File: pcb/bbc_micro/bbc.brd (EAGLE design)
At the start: 52 x 55 mm, 16 parts, among them J1 ATX24RH

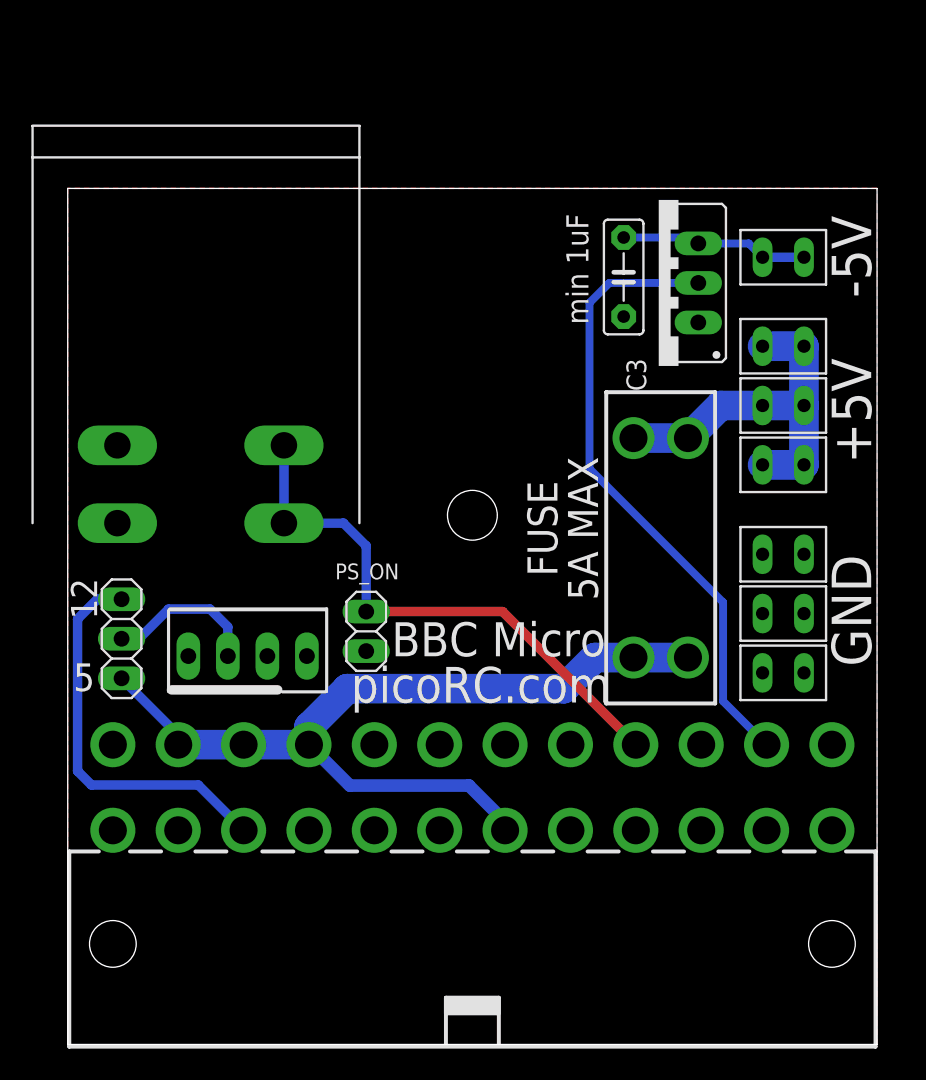
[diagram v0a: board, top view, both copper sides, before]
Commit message: added one more -5v rail
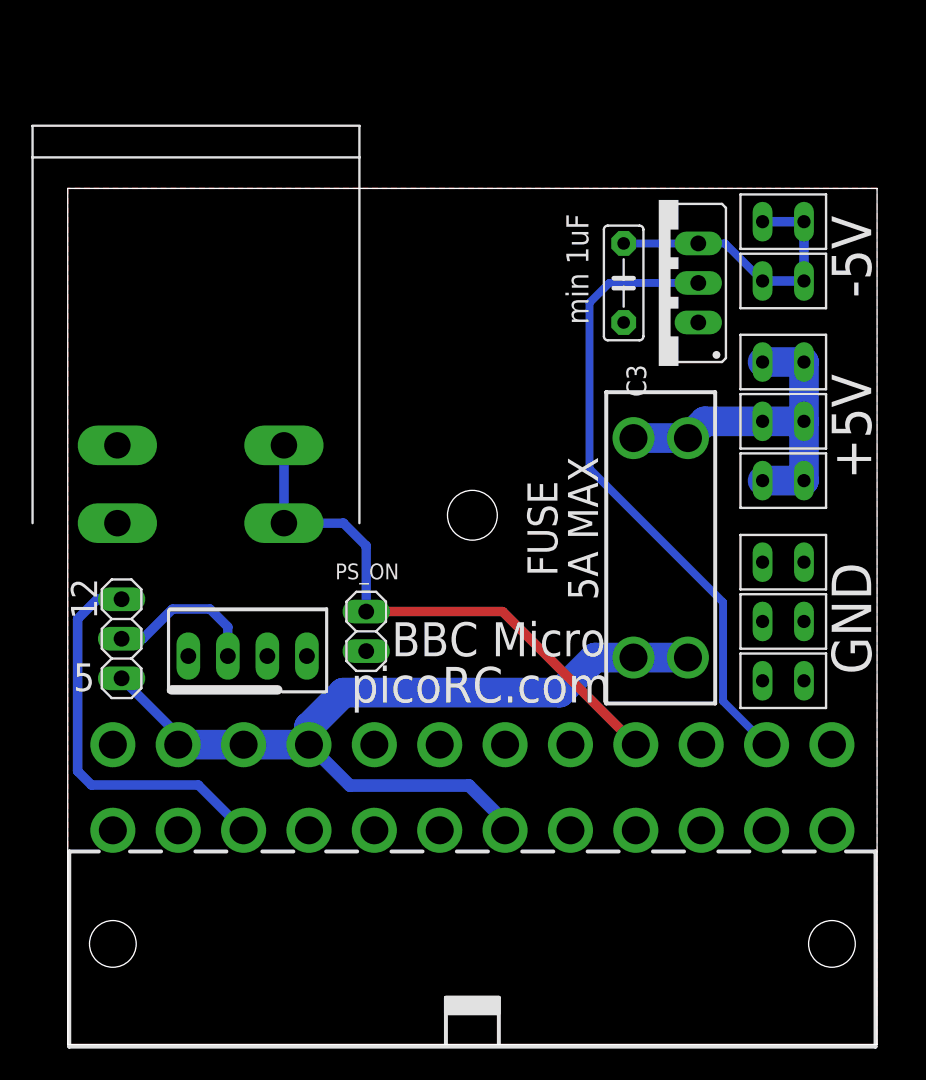
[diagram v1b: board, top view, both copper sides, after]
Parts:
- added U$5: BLADE28, blade:2.8BLADE
- moved U$2 1.52 mm to (46.0, 43.1)
- moved U$6 1.02 mm to (46.0, 37.8)
- moved U$8 1.02 mm to (46.0, 30.2)
- moved U$7 1.02 mm to (46.0, 34.0)
- moved U$9 0.51 mm to (46.0, 25.0)
- moved U$10 0.51 mm to (46.0, 21.2)
- moved U$11 0.51 mm to (46.0, 17.4)
- moved C3 0.38 mm to (35.7, 42.9)
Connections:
- net N$2: now also U$5.P$1, U$5.P$2
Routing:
- net N$2: track 12.1 -> 19.1 mm

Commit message: finishing touches
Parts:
- moved JP1 11.6 mm to (12.7, 30.1), turned to 180 degrees
- moved U$3 6.00 mm to (8.24, 33.5)
- moved C3 6.00 mm to (35.7, 48.9)
- moved IC1 6.00 mm to (38.0, 48.9)
- moved J1 6.00 mm to (26.0, 9.00)
- moved JP2 6.00 mm to (3.46, 26.1)
- moved JP3 6.00 mm to (11.6, 25.0)
- moved U$1 6.00 mm to (38.1, 31.9)
- moved U$10 6.00 mm to (46.0, 27.2)
- moved U$11 6.00 mm to (46.0, 23.4)
- moved U$2 6.00 mm to (46.0, 49.1)
- moved U$4 6.00 mm to (26.0, 34.0)
- moved U$5 6.00 mm to (46.0, 52.9)
- moved U$6 6.00 mm to (46.0, 43.8)
- moved U$7 6.00 mm to (46.0, 40.0)
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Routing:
- net -12V: track 40.6 -> 39.9 mm
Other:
- outline, holes or cut-outs redrawn
